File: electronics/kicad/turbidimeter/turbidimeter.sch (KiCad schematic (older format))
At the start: 7 parts, among them U1 74HC595, U17 74HC595, U19 CD74HC4067M

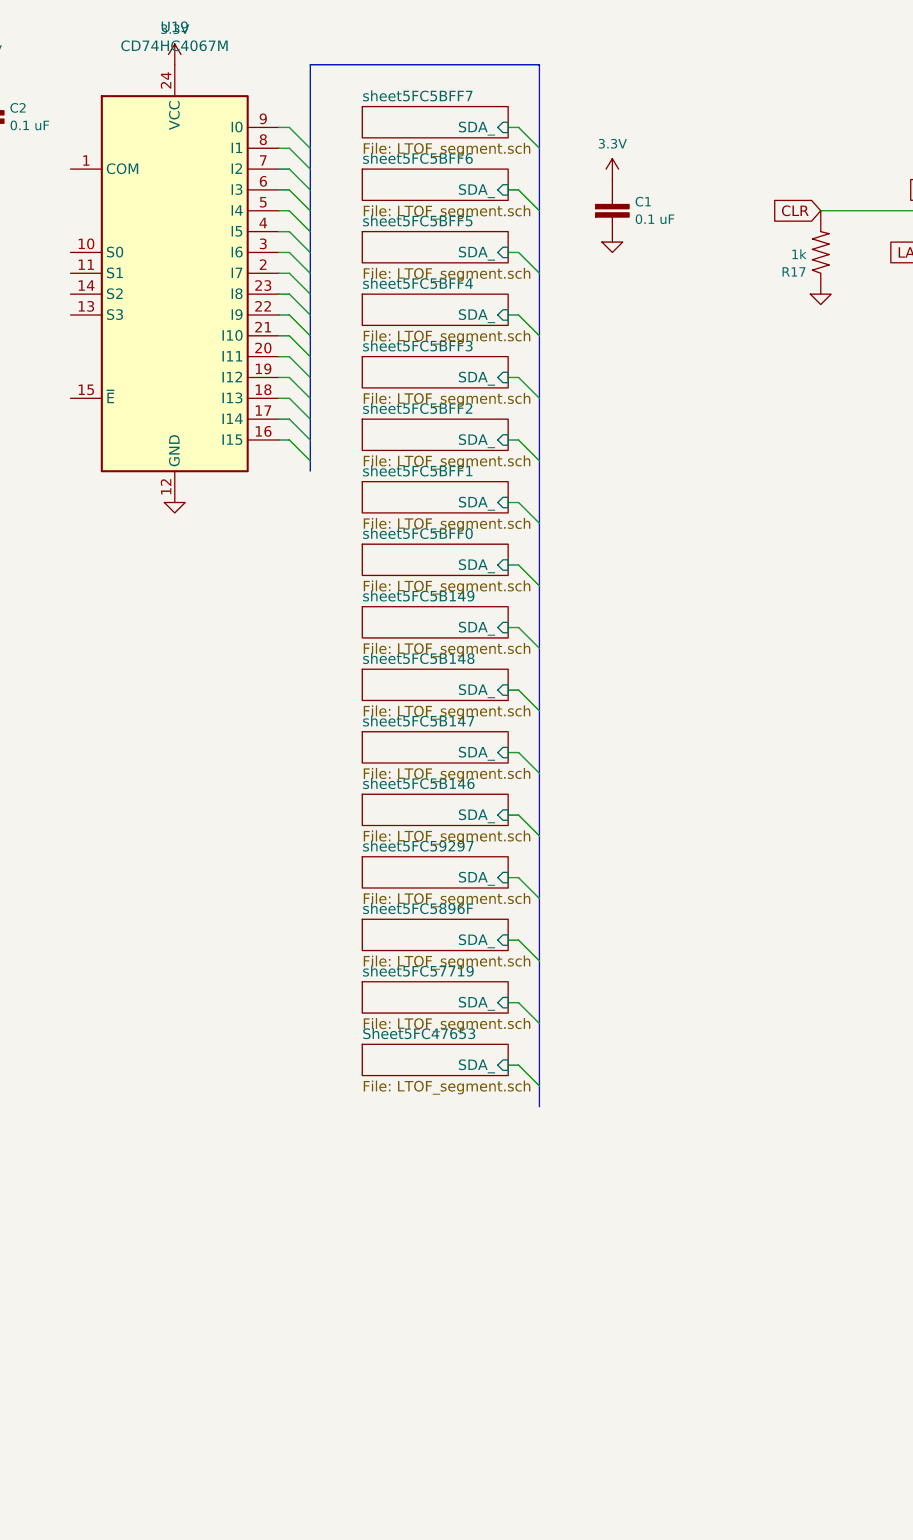
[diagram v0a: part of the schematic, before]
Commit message: Simple absorption/reflection calc
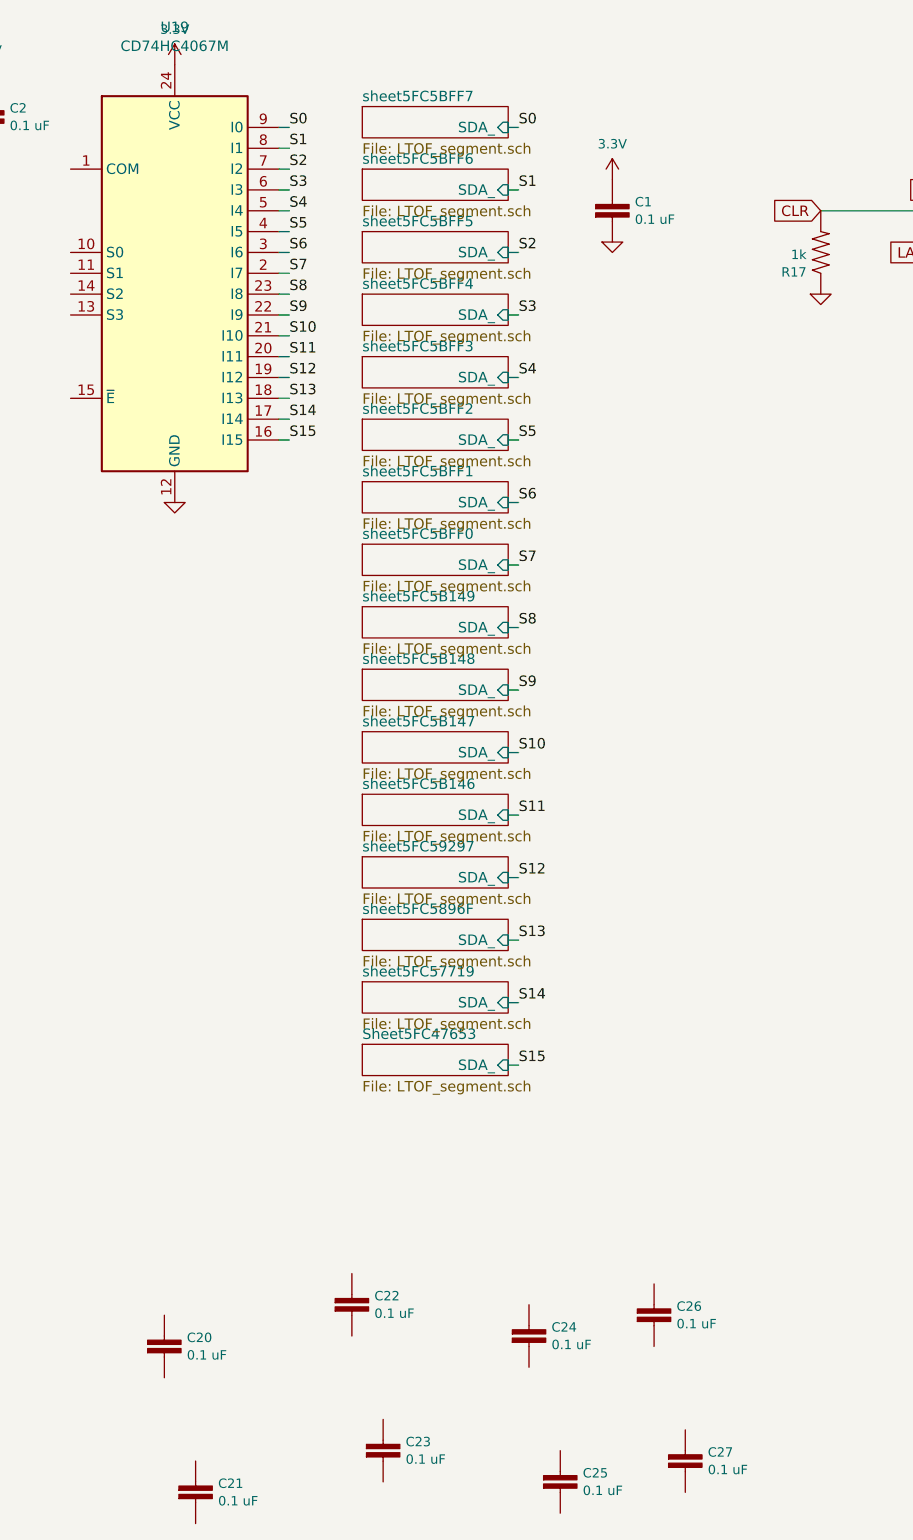
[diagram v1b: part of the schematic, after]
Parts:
- added C20, C21, C22, C23, C24, C25, C26, C27: 0.1 uF, 0603, symbol SparkFun-Capacitors:0.1UF-0603-25V-5%
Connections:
- net S15: now reaches U19.16 (I15)
- net S14: now reaches U19.17 (I14)
- net S13: now reaches U19.18 (I13)
- net S12: now reaches U19.19 (I12)
- net S7: now reaches U19.2 (I7)
- net S11: now reaches U19.20 (I11)
- net S10: now reaches U19.21 (I10)
- net S9: now reaches U19.22 (I9)
- net S8: now reaches U19.23 (I8)
- net S6: now reaches U19.3 (I6)
- net S5: now reaches U19.4 (I5)
- net S4: now reaches U19.5 (I4)
- net S3: now reaches U19.6 (I3)
- net S2: now reaches U19.7 (I2)
- net S1: now reaches U19.8 (I1)
- net S0: now reaches U19.9 (I0)
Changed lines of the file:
@@
-$EndSheet
-$Sheet
-S 2650 3900 700  150
-U 5FC5B14F
-F0 "sheet5FC5B147" 50
-F1 "LTOF_segment.sch" 50
-F2 "SDA_" I R 3350 4000 50
 $EndSheet
 $Sheet
@@
 $EndSheet
 $Sheet
-S 2650 2700 700  150
-U 5FC5BFFD
-F0 "sheet5FC5BFF1" 50
-F1 "LTOF_segment.sch" 50
-F2 "SDA_" I R 3350 2800 50
-$EndSheet
-$Sheet
 S 2650 2400 700  150
 U 5FC5C000
@@
 F2 "SDA_" I R 3350 1000 50
 $EndSheet
-Wire Bus Line
-	2400 700  3500 700
-Entry Wire Line
-	3400 4900 3500 5000
-Entry Wire Line
-	3400 1000 3500 1100
-Entry Wire Line
-	3400 1300 3500 1400
-Entry Wire Line
-	3400 1600 3500 1700
-Entry Wire Line
-	3400 1900 3500 2000
-Entry Wire Line
-	3400 2200 3500 2300
-Entry Wire Line
-	3400 2500 3500 2600
-Entry Wire Line
-	3400 2800 3500 2900
-Entry Wire Line
-	3400 3100 3500 3200
-Entry Wire Line
-	3400 3400 3500 3500
-Entry Wire Line
-	3400 3700 3500 3800
-Entry Wire Line
-	3400 4000 3500 4100
-Entry Wire Line
-	3400 4300 3500 4400
-Entry Wire Line
-	3400 4600 3500 4700
-Entry Wire Line
-	3400 5200 3500 5300
-Entry Wire Line
-	3400 5500 3500 5600
 Wire Wire Line
 	2250 1000 2300 1000
-Entry Wire Line
-	2300 1000 2400 1100
 Wire Wire Line
 	3350 1000 3400 1000
@@
 Wire Wire Line
 	3350 5500 3400 5500
-Entry Wire Line
-	2300 1100 2400 1200
-Entry Wire Line
-	2300 1200 2400 1300
-Entry Wire Line
-	2300 1300 2400 1400
-Entry Wire Line
-	2300 1400 2400 1500
-Entry Wire Line
-	2300 1500 2400 1600
-Entry Wire Line
-	2300 1600 2400 1700
-Entry Wire Line
-	2300 1700 2400 1800
-Entry Wire Line
-	2300 1800 2400 1900
-Entry Wire Line
-	2300 1900 2400 2000
-Entry Wire Line
-	2300 2000 2400 2100
-Entry Wire Line
-	2300 2100 2400 2200
-Entry Wire Line
-	2300 2200 2400 2300
-Entry Wire Line
-	2300 2300 2400 2400
-Entry Wire Line
-	2300 2400 2400 2500
-Entry Wire Line
-	2300 2500 2400 2600
 Wire Wire Line
 	2250 1100 2300 1100
@@
 Wire Wire Line
 	8500 1350 8050 1350
-Wire Bus Line
-	2400 700  2400 2650
-Wire Bus Line
-	3500 700  3500 5700
 Text GLabel 8500 1250 0    50   Input ~ 0
 CLK
 Text GLabel 5500 1300 0    50   Input ~ 0
 CLK
+$Sheet
+S 2650 3900 700  150
+U 5FC5B14F
+F0 "sheet5FC5B147" 50
+F1 "LTOF_segment.sch" 50
+F2 "SDA_" I R 3350 4000 50
+$EndSheet
+$Sheet
+S 2650 2700 700  150
+U 5FC5BFFD
+F0 "sheet5FC5BFF1" 50
+F1 "LTOF_segment.sch" 50
+F2 "SDA_" I R 3350 2800 50
+$EndSheet
+Text Label 2300 1000 0    50   ~ 0
+S0
+Text Label 2300 1100 0    50   ~ 0
+S1
+Text Label 2300 1200 0    50   ~ 0
+S2
+Text Label 2300 1300 0    50   ~ 0
+S3
+Text Label 2300 1400 0    50   ~ 0
+S4
+Text Label 2300 1500 0    50   ~ 0
+S5
+Text Label 2300 1600 0    50   ~ 0
+S6
+Text Label 2300 1700 0    50   ~ 0
+S7
+Text Label 2300 1800 0    50   ~ 0
+S8
+Text Label 2300 1900 0    50   ~ 0
+S9
+Text Label 2300 2000 0    50   ~ 0
+S10
+Text Label 2300 2100 0    50   ~ 0
+S11
+Text Label 2300 2200 0    50   ~ 0
+S12
+Text Label 2300 2300 0    50   ~ 0
+S13
+Text Label 2300 2400 0    50   ~ 0
+S14
+Text Label 2300 2500 0    50   ~ 0
+S15
+Text Label 3400 1000 0    50   ~ 0
+S0
+Text Label 3400 1300 0    50   ~ 0
+S1
+Text Label 3400 1600 0    50   ~ 0
+S2
+Text Label 3400 1900 0    50   ~ 0
+S3
+Text Label 3400 2200 0    50   ~ 0
+S4
+Text Label 3400 2500 0    50   ~ 0
+S5
+Text Label 3400 2800 0    50   ~ 0
+S6
+Text Label 3400 3100 0    50   ~ 0
+S7
+Text Label 3400 3400 0    50   ~ 0
+S8
+Text Label 3400 3700 0    50   ~ 0
+S9
+Text Label 3400 4000 0    50   ~ 0
+S10
+Text Label 3400 4300 0    50   ~ 0
+S11
+Text Label 3400 4600 0    50   ~ 0
+S12
+Text Label 3400 4900 0    50   ~ 0
+S13
+Text Label 3400 5200 0    50   ~ 0
+S14
+Text Label 3400 5500 0    50   ~ 0
+S15
+$Comp
+L SparkFun-Capacitors:0.1UF-0603-25V-5% C21
+U 1 1 5FCF4ECB
+P 1850 7600
+F 0 "C21" H 1958 7692 45  0000 L CNN
+F 1 "0.1 uF" H 1958 7608 45  0000 L CNN
+F 2 "0603" H 1850 7850 20  0001 C CNN
+F 3 "" H 1850 7600 50  0001 C CNN
+F 4 "" H 1958 7566 60  0000 L CNN "Field4"
+	1    1850 7600
+	1    0    0    -1
+$EndComp
+$Comp
+L SparkFun-Capacitors:0.1UF-0603-25V-5% C23
+U 1 1 5FCF566E
+P 2750 7400
+F 0 "C23" H 2858 7492 45  0000 L CNN
+F 1 "0.1 uF" H 2858 7408 45  0000 L CNN
+F 2 "0603" H 2750 7650 20  0001 C CNN
+F 3 "" H 2750 7400 50  0001 C CNN
+F 4 "" H 2858 7366 60  0000 L CNN "Field4"
+	1    2750 7400
+	1    0    0    -1
+$EndComp
+$Comp
+L SparkFun-Capacitors:0.1UF-0603-25V-5% C25
+U 1 1 5FCF5955
+P 3600 7550
+F 0 "C25" H 3708 7642 45  0000 L CNN
+F 1 "0.1 uF" H 3708 7558 45  0000 L CNN
+F 2 "0603" H 3600 7800 20  0001 C CNN
+F 3 "" H 3600 7550 50  0001 C CNN
+F 4 "" H 3708 7516 60  0000 L CNN "Field4"
+	1    3600 7550
+	1    0    0    -1
+$EndComp
+$Comp
+L SparkFun-Capacitors:0.1UF-0603-25V-5% C27
+U 1 1 5FCF5BC4
+P 4200 7450
+F 0 "C27" H 4308 7542 45  0000 L CNN
+F 1 "0.1 uF" H 4308 7458 45  0000 L CNN
+F 2 "0603" H 4200 7700 20  0001 C CNN
+F 3 "" H 4200 7450 50  0001 C CNN
+F 4 "" H 4308 7416 60  0000 L CNN "Field4"
+	1    4200 7450
+	1    0    0    -1
+$EndComp
+$Comp
+L SparkFun-Capacitors:0.1UF-0603-25V-5% C20
+U 1 1 5FCF72A9
+P 1700 6900
+F 0 "C20" H 1808 6992 45  0000 L CNN
+F 1 "0.1 uF" H 1808 6908 45  0000 L CNN
+F 2 "0603" H 1700 7150 20  0001 C CNN
+F 3 "" H 1700 6900 50  0001 C CNN
+F 4 "" H 1808 6866 60  0000 L CNN "Field4"
+	1    1700 6900
+	1    0    0    -1
+$EndComp
+$Comp
+L SparkFun-Capacitors:0.1UF-0603-25V-5% C22
+U 1 1 5FCF72B0
+P 2600 6700
+F 0 "C22" H 2708 6792 45  0000 L CNN
+F 1 "0.1 uF" H 2708 6708 45  0000 L CNN
+F 2 "0603" H 2600 6950 20  0001 C CNN
+F 3 "" H 2600 6700 50  0001 C CNN
+F 4 "" H 2708 6666 60  0000 L CNN "Field4"
+	1    2600 6700
+	1    0    0    -1
+$EndComp
+$Comp
+L SparkFun-Capacitors:0.1UF-0603-25V-5% C24
+U 1 1 5FCF72B7
+P 3450 6850
+F 0 "C24" H 3558 6942 45  0000 L CNN
+F 1 "0.1 uF" H 3558 6858 45  0000 L CNN
+F 2 "0603" H 3450 7100 20  0001 C CNN
+F 3 "" H 3450 6850 50  0001 C CNN
+F 4 "" H 3558 6816 60  0000 L CNN "Field4"
+	1    3450 6850
+	1    0    0    -1
+$EndComp
+$Comp
+L SparkFun-Capacitors:0.1UF-0603-25V-5% C26
+U 1 1 5FCF72BE
+P 4050 6750
+F 0 "C26" H 4158 6842 45  0000 L CNN
+F 1 "0.1 uF" H 4158 6758 45  0000 L CNN
+F 2 "0603" H 4050 7000 20  0001 C CNN
+F 3 "" H 4050 6750 50  0001 C CNN
+F 4 "" H 4158 6716 60  0000 L CNN "Field4"
+	1    4050 6750
+	1    0    0    -1
+$EndComp
 $EndSCHEMATC

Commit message: turbidimeter
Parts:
- removed C20, C21, C22, C23, C24, C25, C26, C27, C3: 0.1 uF, 0603, symbol SparkFun-Capacitors:0.1UF-0603-25V-5%
- removed U1: 74HC595, Package_SO:SOIC-16_3.9x9.9mm_P1.27mm, symbol 74xx:74HC595
- added P1, P2, P3: CONN_6, Connectors2:1X06-SMD-FEMALE, symbol conn:CONN_6
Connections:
- net 3.3V: now also P1.5, P3.5
- net CLK: now also P1.1
- net CLR: now also P1.2
- net GND: now also U19.15 (~E), P1.6, P3.6
- net LATCH: now also P1.3
- net SDA: now reaches U19.1 (COM)
- net SDA: now also P2.3
- net A1: now reaches U19.10 (S0)
- net A1: now also P2.4
- net A0: now reaches U19.11 (S1)
- net A0: now also P2.5
- net A3: now reaches U19.13 (S3)
- net A3: now also P2.1
- net A2: now reaches U19.14 (S2)
- net A2: now also P2.2
- net SER: now reaches U17.14 (SER)
- net SER: now also P1.4
- new net SCL: P2.6
